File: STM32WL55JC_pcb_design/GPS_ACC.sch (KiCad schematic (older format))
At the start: 9 parts

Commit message: First pcb commit
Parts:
- U?: symbol L80-M39:L80-M39 -> STM32WL55JC_pcb_design-rescue:L80-M39-L80-M39
- U?: symbol LIS3DHTR:LIS3DHTR -> STM32WL55JC_pcb_design-rescue:LIS3DHTR-LIS3DHTR
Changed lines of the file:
@@
 $EndDescr
 $Comp
-L L80-M39:L80-M39 U?
+L STM32WL55JC_pcb_design-rescue:L80-M39-L80-M39 U?
 U 1 1 61322FDC
 P 5750 4450
@@
 $EndComp
 $Comp
-L LIS3DHTR:LIS3DHTR U?
+L STM32WL55JC_pcb_design-rescue:LIS3DHTR-LIS3DHTR U?
 U 1 1 61322FE6
 P 5800 2800

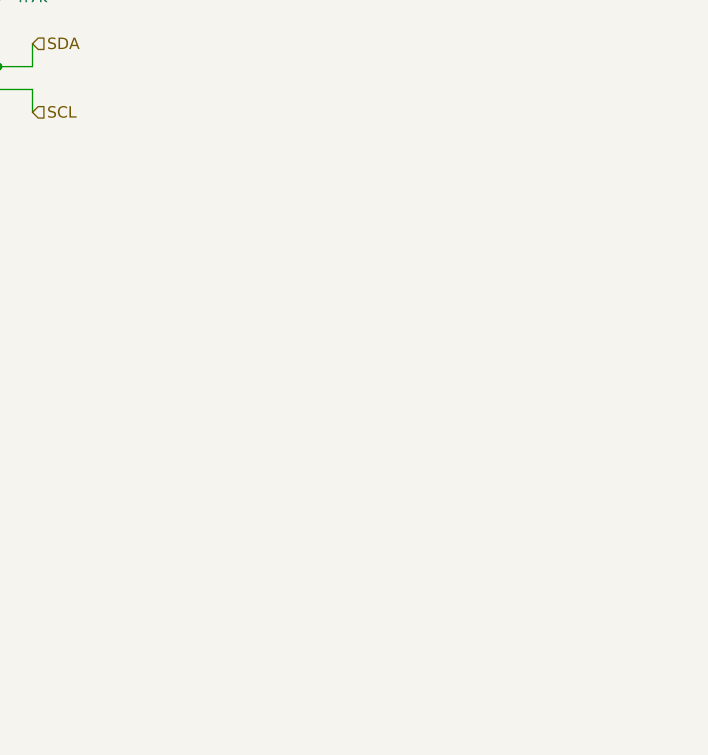
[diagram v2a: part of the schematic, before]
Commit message: Add temperature and humidty sensor, add rf connections
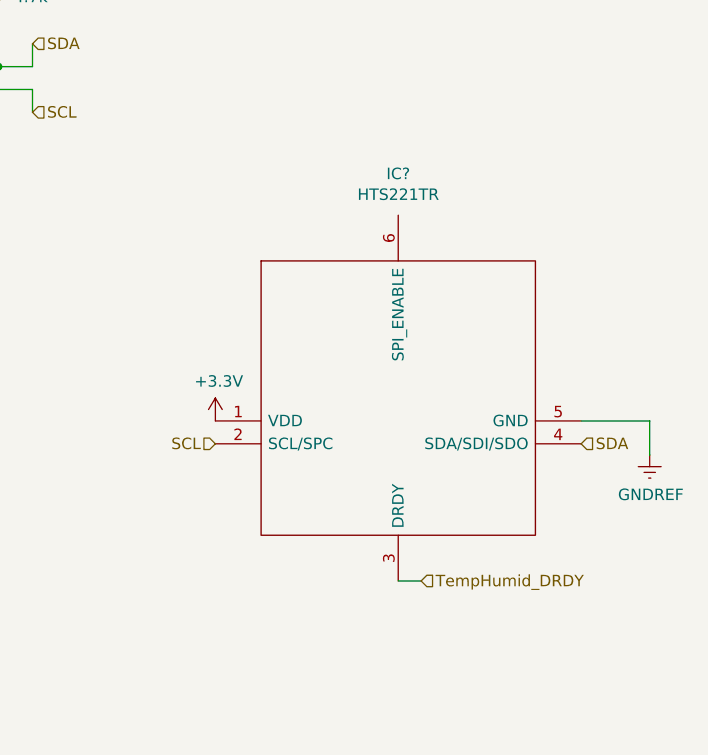
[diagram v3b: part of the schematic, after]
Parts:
- added IC?: HTS221TR, HLGA-6L, symbol HTS221TR:HTS221TR
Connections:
- net +3V3: now also IC?.1 (VDD)
- net GNDREF: now also IC?.5 (GND)
- net SCL: now also IC?.2 (SCL/SPC)
- net SDA: now also IC?.4 (SDA/SDI/SDO)
- new net TempHumid_DRDY: IC?.3 (DRDY)
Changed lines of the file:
@@
 $Descr A4 11693 8268
 encoding utf-8
-Sheet 3 5
+Sheet 3 6
 Title ""
 Date ""
@@
 Text HLabel 6600 4350 2    50   Input ~ 0
 RX
+$Comp
+L HTS221TR:HTS221TR IC?
+U 1 1 6141EBB5
+P 8000 4050
+F 0 "IC?" H 8800 5131 50  0000 C CNN
+F 1 "HTS221TR" H 8800 5040 50  0000 C CNN
+F 2 "HLGA-6L" H 9450 4750 50  0001 L CNN
+F 3 "http://www.st.com/content/ccc/resource/technical/document/datasheet/4d/9a/9c/ad/25/07/42/34/DM00116291.pdf/files/DM00116291.pdf/jcr:content/translations/en.DM00116291.pdf" H 9450 4650 50  0001 L CNN
+F 4 "Humidity and Temperature Sensor HLGA6 STMicroelectronics HTS221TR Temperature & Humidity Sensor, -40  +120 C, 6-Pin HLGA" H 9450 4550 50  0001 L CNN "Description"
+F 5 "" H 9450 4450 50  0001 L CNN "Height"
+F 6 "STMicroelectronics" H 9450 4350 50  0001 L CNN "Manufacturer_Name"
+F 7 "HTS221TR" H 9450 4250 50  0001 L CNN "Manufacturer_Part_Number"
+F 8 "511-HTS221TR" H 9450 4150 50  0001 L CNN "Mouser Part Number"
+F 9 "https://www.mouser.co.uk/ProductDetail/STMicroelectronics/HTS221TR?qs=9MuLHSklicqAHntRLffjZQ%3D%3D" H 9450 4050 50  0001 L CNN "Mouser Price/Stock"
+F 10 "HTS221TR" H 9450 3950 50  0001 L CNN "Arrow Part Number"
+F 11 "https://www.arrow.com/en/products/hts221tr/stmicroelectronics" H 9450 3850 50  0001 L CNN "Arrow Price/Stock"
+	1    8000 4050
+	1    0    0    -1
+$EndComp
+Text HLabel 9600 4150 2    50   Input ~ 0
+SDA
+Text HLabel 8000 4150 0    50   Input ~ 0
+SCL
+$Comp
+L power:+3.3V #PWR?
+U 1 1 61420A78
+P 8000 4050
+AR Path="/61420A78" Ref="#PWR?"  Part="1"
+AR Path="/61317136/61420A78" Ref="#PWR?"  Part="1"
+F 0 "#PWR?" H 8000 3900 50  0001 C CNN
+F 1 "+3.3V" H 8015 4223 50  0000 C CNN
+F 2 "" H 8000 4050 50  0001 C CNN
+F 3 "" H 8000 4050 50  0001 C CNN
+	1    8000 4050
+	1    0    0    -1
+$EndComp
+Wire Wire Line
+	9600 4050 9900 4050
+Wire Wire Line
+	9900 4050 9900 4200
+$Comp
+L power:GNDREF #PWR?
+U 1 1 61421FD9
+P 9900 4200
+AR Path="/61421FD9" Ref="#PWR?"  Part="1"
+AR Path="/61317136/61421FD9" Ref="#PWR?"  Part="1"
+F 0 "#PWR?" H 9900 3950 50  0001 C CNN
+F 1 "GNDREF" H 9905 4027 50  0000 C CNN
+F 2 "" H 9900 4200 50  0001 C CNN
+F 3 "" H 9900 4200 50  0001 C CNN
+	1    9900 4200
+	1    0    0    -1
+$EndComp
+Wire Wire Line
+	8800 4750 8900 4750
+Text HLabel 8900 4750 2    50   Input ~ 0
+TempHumid_DRDY
 $EndSCHEMATC
